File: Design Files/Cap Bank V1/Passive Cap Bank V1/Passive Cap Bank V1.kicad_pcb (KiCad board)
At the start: 2 copper layers, 66.4 x 115.9 mm, 39 parts, among them J1 XT30-Male, Q1 BC817-40, Q2 BC817-40, Q3 BC817-40, Q4 BC817-40, Q5 BC817-40, Q6 BC817-40, SW1 SW_Push_Open

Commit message: Added missing files
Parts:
- moved D1 28.3 mm to (123.0, 110.0), turned to 180 degrees
- moved R14 28.3 mm to (131.0, 110.1)
- moved R13 14.6 mm to (125.4, 120.4)
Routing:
- net V_15: track 27.4 -> 65.9 mm
- net Net-(D1-A): track 0.00 -> 36.5 mm
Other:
- outline, holes or cut-outs redrawn
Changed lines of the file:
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@@
 	(footprint "PassiveBankV1:680 Resistor"
 		(layer "F.Cu")
-		(at 131.5212 138.3538 90)
+		(at 131.0165 110.05197 90)
 		(tags "LR1F680R ")
 		(property "Reference" "R14"
@@
 	(footprint "PassiveBankV1:10mm LED"
 		(layer "F.Cu")
-		(at 123.476312 138.257212)
+		(at 122.971612 109.955382 180)
 		(tags "WP813SURDK ")
 		(property "Reference" "D1"
-			(at -6.001012 -4.061012 0)
+			(at -6.001012 -4.061012 180)
 			(unlocked yes)
 			(layer "F.SilkS")
@@
 		)
 		(property "Value" "10mm_LED"
-			(at 0.192988 2.453588 0)
+			(at 0.192988 2.453588 180)
 			(unlocked yes)
 			(layer "F.Fab")
@@
 		)
 		(property "Footprint" "PassiveBankV1:10mm LED"
-			(at -1.331012 -7.62 0)
+			(at -1.331012 -7.62 360)
 			(layer "F.Fab")
 			(hide yes)
@@
 		)
 		(property "Datasheet" ""
-			(at -1.331012 -0.061012 0)
+			(at -1.331012 -0.061012 360)
 			(layer "F.Fab")
 			(hide yes)
@@
 		)
 		(property "Description" "Light emitting diode"
-			(at 0 7.62 0)
+			(at 0 7.62 360)
 			(layer "F.Fab")
 			(hide yes)
@@
 		(attr through_hole)
 		(fp_line
-			(start -3.251 -0.625)
-			(end -3.251 0.645)
+			(start -2.235 0.01)
+			(end -3.505 0.01)
 			(stroke
 				(width 0.1524)
@@
 		)
 		(fp_line
-			(start -3.251 0.01)
-			(end -2.489 -0.625)
+			(start -2.489 -0.625)
+			(end -2.489 0.645)
 			(stroke
 				(width 0.1524)
@@
 		(fp_line
 			(start -3.251 0.01)
-			(end -2.489 -0.498)
+			(end -2.489 0.645)
 			(stroke
 				(width 0.1524)
@@
 		(fp_line
 			(start -3.251 0.01)
-			(end -2.489 -0.371)
+			(end -2.489 0.518)
 			(stroke
 				(width 0.1524)
@@
 		(fp_line
 			(start -3.251 0.01)
-			(end -2.489 -0.244)
+			(end -2.489 0.391)
 			(stroke
 				(width 0.1524)
@@
 		(fp_line
 			(start -3.251 0.01)
-			(end -2.489 -0.117)
+			(end -2.489 0.264)
 			(stroke
 				(width 0.1524)
@@
 		(fp_line
 			(start -3.251 0.01)
-			(end -2.489 0.264)
+			(end -2.489 -0.117)
 			(stroke
 				(width 0.1524)
@@
 		(fp_line
 			(start -3.251 0.01)
-			(end -2.489 0.391)
+			(end -2.489 -0.244)
 			(stroke
 				(width 0.1524)
@@
 		(fp_line
 			(start -3.251 0.01)
-			(end -2.489 0.518)
+			(end -2.489 -0.371)
 			(stroke
 				(width 0.1524)
@@
 		(fp_line
 			(start -3.251 0.01)
-			(end -2.489 0.645)
+			(end -2.489 -0.498)
 			(stroke
 				(width 0.1524)
@@
 		)
 		(fp_line
-			(start -2.489 -0.625)
-			(end -2.489 0.645)
+			(start -3.251 0.01)
+			(end -2.489 -0.625)
 			(stroke
 				(width 0.1524)
@@
 		)
 		(fp_line
-			(start -2.235 0.01)
-			(end -3.505 0.01)
+			(start -3.251 -0.625)
+			(end -3.251 0.645)
 			(stroke
 				(width 0.1524)
@@
 		)
 		(fp_line
-			(start -5.814112 -2.429935)
-			(end -2.429935 -5.814112)
+			(start 5.692088 2.307911)
+			(end 2.307911 5.692088)
 			(stroke
 				(width 0.0254)
@@
 		)
 		(fp_line
-			(start -5.814112 2.307911)
-			(end -5.814112 -2.429935)
+			(start 5.692088 -2.429935)
+			(end 5.692088 2.307911)
 			(stroke
 				(width 0.0254)
@@
 		)
 		(fp_line
-			(start -2.429935 -5.814112)
-			(end 2.307911 -5.814112)
+			(start 2.307911 5.692088)
+			(end -2.429935 5.692088)
 			(stroke
 				(width 0.0254)
@@
 		)
 		(fp_line
-			(start -2.429935 5.692088)
-			(end -5.814112 2.307911)
+			(start 2.307911 -5.814112)
+			(end 5.692088 -2.429935)
 			(stroke
 				(width 0.0254)
@@
 		)
 		(fp_line
-			(start 2.307911 -5.814112)
-			(end 5.692088 -2.429935)
+			(start -2.429935 5.692088)
+			(end -5.814112 2.307911)
 			(stroke
 				(width 0.0254)
@@
 		)
 		(fp_line
-			(start 2.307911 5.692088)
-			(end -2.429935 5.692088)
+			(start -2.429935 -5.814112)
+			(end 2.307911 -5.814112)
 			(stroke
 				(width 0.0254)
@@
 		)
 		(fp_line
-			(start 5.692088 -2.429935)
-			(end 5.692088 2.307911)
+			(start -5.814112 2.307911)
+			(end -5.814112 -2.429935)
 			(stroke
 				(width 0.0254)
@@
 		)
 		(fp_line
-			(start 5.692088 2.307911)
-			(end 2.307911 5.692088)
+			(start -5.814112 -2.429935)
+			(end -2.429935 -5.814112)
 			(stroke
 				(width 0.0254)
@@
 		)
 		(fp_line
-			(start -3.251 -0.625)
-			(end -3.251 0.645)
+			(start -2.235 0.01)
+			(end -3.505 0.01)
 			(stroke
 				(width 0.0254)
@@
 		)
 		(fp_line
-			(start -3.251 0.01)
-			(end -2.489 -0.625)
+			(start -2.489 -0.625)
+			(end -2.489 0.645)
 			(stroke
 				(width 0.0254)
@@
 		(fp_line
 			(start -3.251 0.01)
-			(end -2.489 -0.498)
+			(end -2.489 0.645)
 			(stroke
 				(width 0.0254)
@@
 		(fp_line
 			(start -3.251 0.01)
-			(end -2.489 -0.371)
+			(end -2.489 0.518)
 			(stroke
 				(width 0.0254)
@@
 		(fp_line
 			(start -3.251 0.01)
-			(end -2.489 -0.244)
+			(end -2.489 0.391)
 			(stroke
 				(width 0.0254)
@@
 		(fp_line
 			(start -3.251 0.01)
-			(end -2.489 -0.117)
+			(end -2.489 0.264)
 			(stroke
 				(width 0.0254)
@@
 		(fp_line
 			(start -3.251 0.01)
-			(end -2.489 0.264)
+			(end -2.489 -0.117)
 			(stroke
 				(width 0.0254)
@@
 		(fp_line
 			(start -3.251 0.01)
-			(end -2.489 0.391)
+			(end -2.489 -0.244)
 			(stroke
 				(width 0.0254)
@@
 		(fp_line
 			(start -3.251 0.01)
-			(end -2.489 0.518)
+			(end -2.489 -0.371)
 			(stroke
 				(width 0.0254)
@@
 		(fp_line
 			(start -3.251 0.01)
-			(end -2.489 0.645)
+			(end -2.489 -0.498)
 			(stroke
 				(width 0.0254)
@@
 		)
 		(fp_line
-			(start -2.489 -0.625)
-			(end -2.489 0.645)
+			(start -3.251 0.01)
+			(end -2.489 -0.625)
 			(stroke
 				(width 0.0254)
@@
 		)
 		(fp_line
-			(start -2.235 0.01)
-			(end -3.505 0.01)
+			(start -3.251 -0.625)
+			(end -3.251 0.645)
 			(stroke
 				(width 0.0254)
@@
 		)
 		(pad "1" thru_hole rect
-			(at -1.331012 -0.061012)
+			(at -1.331012 -0.061012 180)
 			(size 1.397 1.397)
 			(drill 0.889)
@@
 		)
 		(pad "2" thru_hole circle
-			(at 1.208988 -0.061012)
+			(at 1.208988 -0.061012 180)
 			(size 1.397 1.397)
 			(drill 0.889)
@@
 	(footprint "PassiveBankV1:100Watt2"
 		(layer "F.Cu")
-		(at 125.406598 105.7836)
+		(at 125.433 120.4056)
 		(tags "TEH100M2R00FE ")
 		(property "Reference" "R13"
@@
 	)
 	(gr_rect
-		(start 117.125198 102.986)
-		(end 133.711398 131.111)
+		(start 117.1516 117.608)
+		(end 133.7378 145.733)
 		(stroke
 			(width 0.1)
@@
 	)
 	(gr_rect
-		(start 117.1448 102.9716)
-		(end 133.6548 131.122)
+		(start 117.171202 117.5936)
+		(end 133.681202 145.744)
 		(stroke
 			(width 0.1)
@@
 	)
 	(gr_rect
-		(start 133.069598 130.752)
-		(end 117.069598 109.752)
+		(start 133.096 145.374)
+		(end 117.096 124.374)
 		(stroke
 			(width 0.05)
@@
 	)
 	(gr_circle
-		(center 125.069598 125.752)
-		(end 126.869598 125.752)
+		(center 125.096 140.374)
+		(end 126.896 140.374)
 		(stroke
 			(width 0.1)
@@
 	)
 	(gr_text "Caution!\nArea may be hot!"
-		(at 124.6124 113.9444 -90)
+		(at 124.638802 128.5664 -90)
 		(layer "B.SilkS")
 		(effects
@@
 	)
 	(gr_text "DO NOT EXCEED:\n7A or 15V"
-		(at 88.952 85.4678 0)
+		(at 43.942 34.544 0)
 		(layer "F.SilkS")
 		(effects
@@
 	)
 	(segment
+		(start 129.6152 70.613)
+		(end 161.45 70.613)
+		(width 2.5)
+		(layer "F.Cu")
+		(net 1)
+	)
+	(segment
+		(start 124.9172 75.311)
+		(end 129.6152 70.613)
+		(width 2.5)
+		(layer "F.Cu")
+		(net 1)
+	)
+	(segment
 		(start 168.148 86.821)
 		(end 168.148 77.311)
@@
 	)
 	(segment
+		(start 121.762624 110.016394)
+		(end 121.762624 88.965576)
+		(width 1.25)
+		(layer "F.Cu")
+		(net 9)
+	)
+	(segment
+		(start 120.352 120.4056)
+		(end 120.352 111.427018)
+		(width 1.25)
+		(layer "F.Cu")
+		(net 9)
+	)
+	(segment
+		(start 121.762624 88.965576)
+		(end 124.9172 85.811)
+		(width 1.25)
+		(layer "F.Cu")
+		(net 9)
+	)
+	(segment
+		(start 120.352 111.427018)
+		(end 121.762624 110.016394)
+		(width 1.25)
+		(layer "F.Cu")
+		(net 9)
+	)
+	(segment
 		(start 177.338 97.155)
 		(end 177.338 93.109)
@@
 	)
 	(group ""
-		(members "78e875fa-280a-4364-a444-62b6c4bc07e7" "81237dd6-1eb9-419c-afab-d7f4872a3857"
-			"97b8cce4-845b-4684-9c0c-3a825e2a98a0" "a01802e2-7f5d-4ec9-8de2-6eafd455eae0"
+		(members "0f04ea32-48f0-4e25-9ac5-f99075a6b85a" "1e4e92bc-e340-4c07-b072-a5769ca5a663"
+			"78e875fa-280a-4364-a444-62b6c4bc07e7" "81237dd6-1eb9-419c-afab-d7f4872a3857"
+			"97b8cce4-845b-4684-9c0c-3a825e2a98a0" "98602c75-e7ec-4582-8c43-4ba32a76df60"
+			"a01802e2-7f5d-4ec9-8de2-6eafd455eae0" "be2aa0ee-0055-48c4-af1b-099d30eb508d"
+			"fa20ba75-40d1-4e38-acf5-cd3031efa8c1"
 		)
 	)
@@
 	)
 	(group ""
-		(members "1e4e92bc-e340-4c07-b072-a5769ca5a663" "fa20ba75-40d1-4e38-acf5-cd3031efa8c1")
-	)
-	(group ""

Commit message: Routing done, holes and copper pour todo
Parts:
- R13: moved to B.Cu
- moved G*** 130.2 mm to (140.0, 144.3)
- moved G*** 64.9 mm to (148.3, 54.9)
- moved D1 28.4 mm to (122.8, 138.3)
- moved R14 28.4 mm to (130.8, 138.4)
- moved R13 14.5 mm to (125.7, 105.9)
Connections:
- R13 pad 3: (no net) -> GND
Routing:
- net GND: track 22.4 -> 87.0 mm
- net Net-(D1-A): track 36.5 -> 54.7 mm
- net Net-(D1-K): track 0.00 -> 9.03 mm
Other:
- outline, holes or cut-outs redrawn
- board text added: "DO NOT EXCEED 7A or 15V"
- board text removed: "DO NOT EXCEED: 7A or 15V"

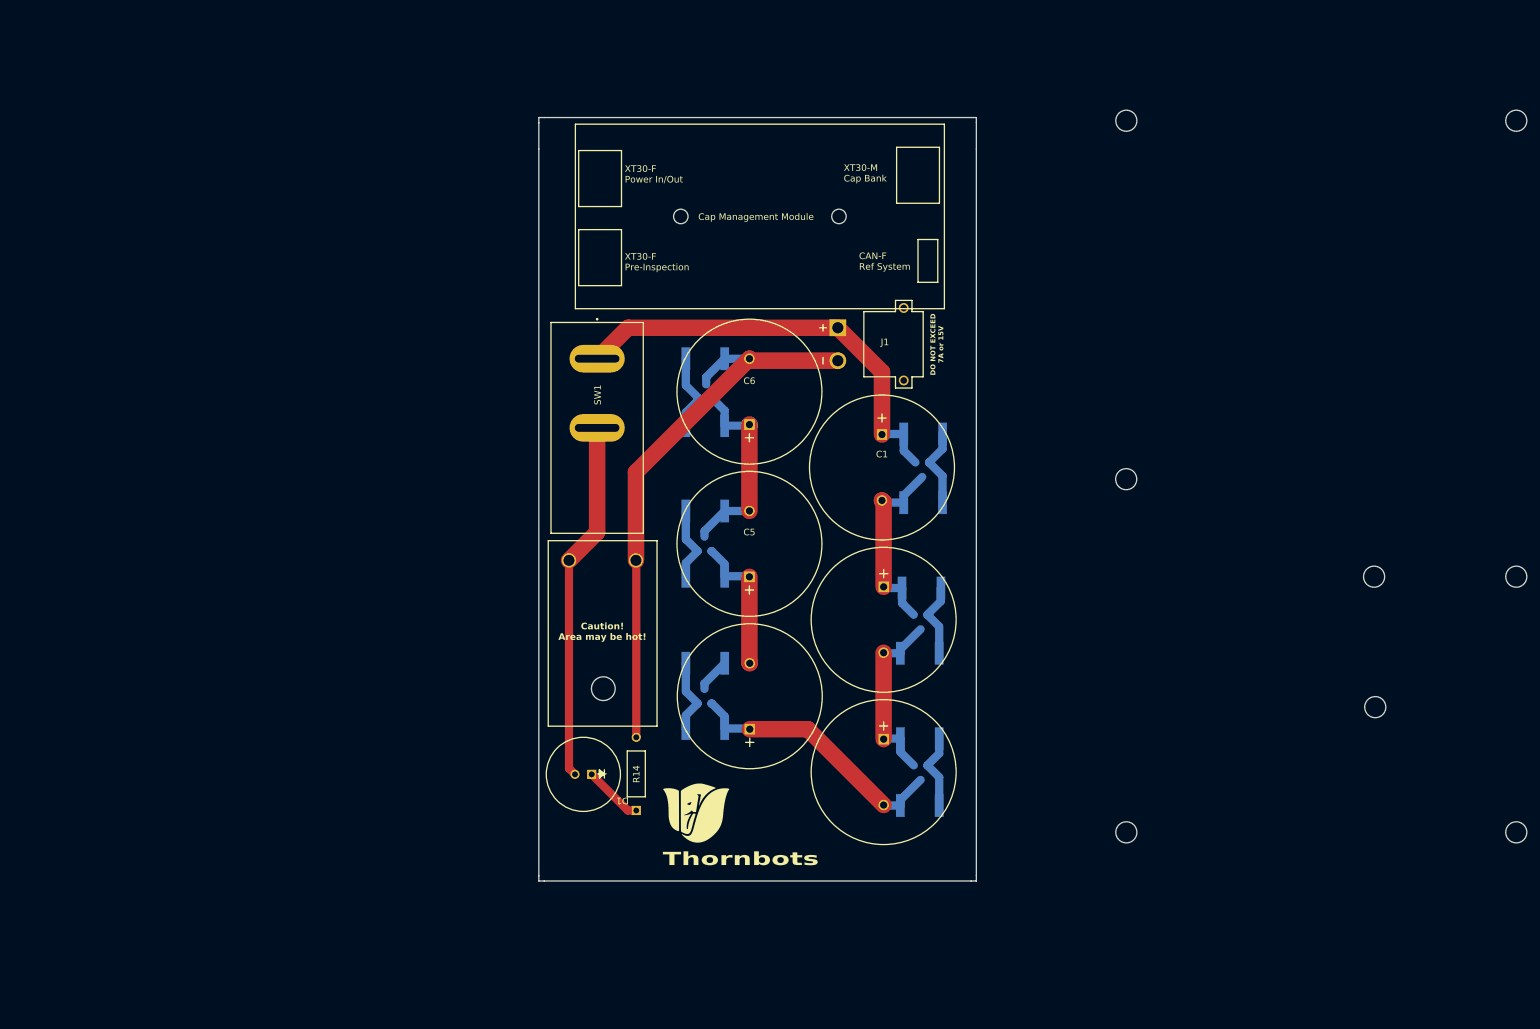
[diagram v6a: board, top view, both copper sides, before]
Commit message: Changed to larger board size, layout wip
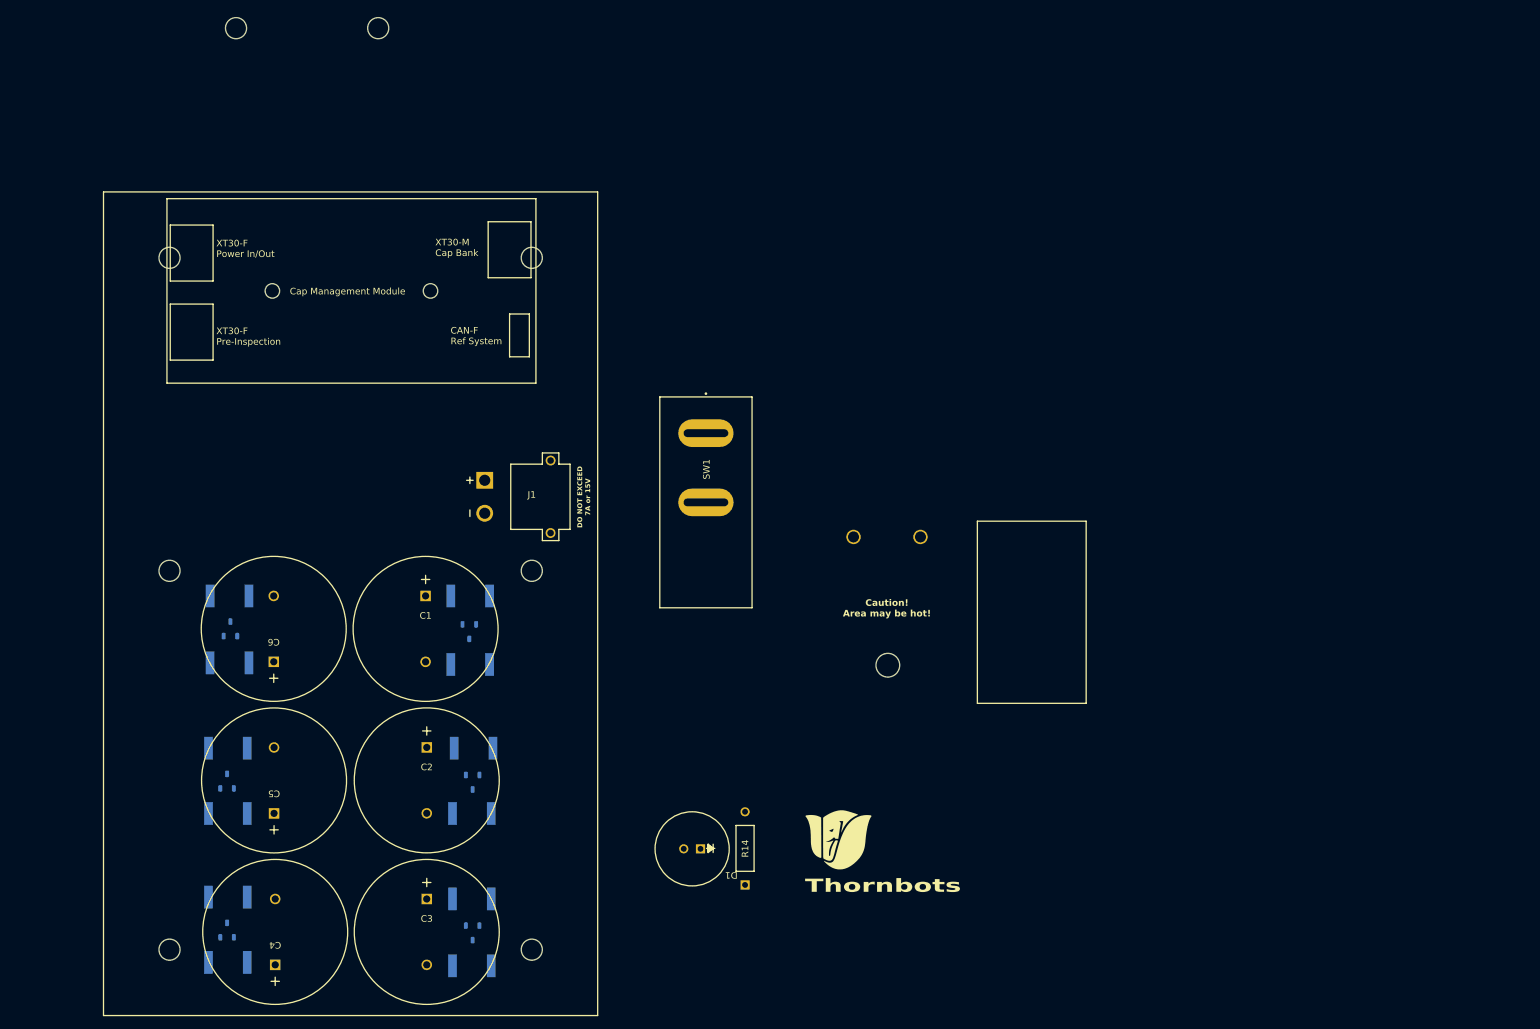
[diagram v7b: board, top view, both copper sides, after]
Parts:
- C1, C2, C3, C4, C5, C6: footprint PassiveBankV1:100F Kyocera Cap -> PGA460TW:100F Kyocera Cap
- moved REF** 191.7 mm to (70.1, 25.1)
- moved REF** 191.7 mm to (91.7, 25.1)
- moved REF** 150.9 mm to (115.0, 60.0)
- moved REF** 150.5 mm to (115.0, 165.0)
- moved REF** 146.7 mm to (60.0, 60.0)
- moved REF** 146.3 mm to (60.0, 165.0)
- moved REF** 145.9 mm to (60.0, 107.5)
- moved REF** 129.7 mm to (115.0, 107.5)
- moved R9 80.9 mm to (68.9, 144.3)
- moved Q5 80.9 mm to (68.8, 139.3)
- moved R10 80.9 mm to (68.9, 134.4)
- moved R7 80.7 mm to (68.9, 166.9)
- moved Q4 80.7 mm to (68.8, 161.9)
- moved R8 80.7 mm to (68.9, 157.0)
- moved C6 80.7 mm to (75.8, 116.3)
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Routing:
- net GND: track 87.0 -> 0.00 mm
- net V_15: track 65.9 -> 0.00 mm
- net Net-(D1-A): track 54.7 -> 0.00 mm
- net Net-(C3--): track 41.4 -> 0.00 mm
- net Net-(C5--): track 30.8 -> 0.00 mm
- net Net-(C1--): track 29.5 -> 0.00 mm
- net Net-(C2--): track 28.1 -> 0.00 mm
- net Net-(C4--): track 26.8 -> 0.00 mm
- net Net-(Q1-B): track 12.1 -> 0.00 mm
- net Net-(Q6-B): track 11.9 -> 0.00 mm
- net Net-(Q3-B): track 11.6 -> 0.00 mm
- net Net-(Q2-B): track 11.5 -> 0.00 mm
- net Net-(Q5-B): track 11.4 -> 0.00 mm
- net Net-(Q4-B): track 11.4 -> 0.00 mm
- net Net-(D1-K): track 9.03 -> 0.00 mm
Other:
- board size 66.4 x 115.9 mm -> 96.3 x 59.7 mm

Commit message: Finished layout and routing. Some Silkscreen to do
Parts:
- moved REF** 109.9 mm to (76.6, 134.9)
- moved REF** 109.6 mm to (100.0, 134.4)
- moved R14 99.3 mm to (61.2, 100.3), turned to 0 degrees
- moved D1 97.2 mm to (61.0, 92.0), turned to 0 degrees
- moved G*** 87.4 mm to (118.5, 72.3)
- moved G*** 78.1 mm to (86.8, 64.5)
- moved R13 74.9 mm to (97.7, 79.1), turned to -90 degrees
- moved SW1 55.3 mm to (86.1, 97.0), turned to 0 degrees
- moved R7 51.5 mm to (60.6, 116.1), turned to 90 degrees
- moved R6 48.0 mm to (60.1, 153.1), turned to 90 degrees
- moved R12 47.4 mm to (116.2, 116.4), turned to -90 degrees
- moved Q4 46.0 mm to (65.7, 116.0), turned to 0 degrees
- moved R1 42.9 mm to (116.2, 152.9), turned to -90 degrees
- moved Q3 42.1 mm to (64.9, 153.3), turned to 180 degrees
- moved Q6 42.1 mm to (111.4, 116.5), turned to 0 degrees
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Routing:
- net GND: track 0.00 -> 100.6 mm
- net V_15: track 0.00 -> 86.1 mm
- net Net-(D1-A): track 0.00 -> 53.8 mm
- net Net-(C3--): track 0.00 -> 41.9 mm
- net Net-(C4--): track 0.00 -> 32.0 mm
- net Net-(C1--): track 0.00 -> 31.1 mm
- net Net-(C2--): track 0.00 -> 30.6 mm
- net Net-(C5--): track 0.00 -> 27.1 mm
- net Net-(Q1-B): track 0.00 -> 12.1 mm
- net Net-(Q6-B): track 0.00 -> 11.9 mm
- net Net-(Q3-B): track 0.00 -> 11.6 mm
- net Net-(Q2-B): track 0.00 -> 11.5 mm
- net Net-(Q4-B): track 0.00 -> 11.4 mm
- net Net-(Q5-B): track 0.00 -> 11.4 mm
- net Net-(D1-K): track 0.00 -> 10.1 mm
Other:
- board size 96.3 x 59.7 mm -> 75 x 125 mm
- board text added: "Add Info on Discharging here! I.e. Switch to left? is discharging, if LED is on, it's currently discharging and has voltage left"
- board text added: "Add some power breakout here!"
- board text added: "T H O R N B O T S"
- board text removed: "Thornbots"
